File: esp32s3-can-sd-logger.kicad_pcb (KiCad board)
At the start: 4 copper layers, 84 x 74 mm, 168 parts, among them J1 PWR + CAN harness, J10 Sensor harness, J2 USB-C, J3 UART0, J4 I2C / Qwiic, J5 SPI, J6 WS2812, J7 Spare IO, J8 Rail break-out, J9 microSD push-pull, Q1 100V 6.8mOhm N-ch, Q2 -20V 2.3A P-ch, Q3 60V 300mA N-ch, SW1 RESET, SW2 BOOT, U1 LM74700-Q1, U2 LM5164 (5V), U3 LM5164 (3V3), U4 ESP32-S3-WROOM-1-N16R8, U5 USBLC6-2SC6, U6 74AHCT1G125, U7 TJA1051T/3, U8 ADS1115

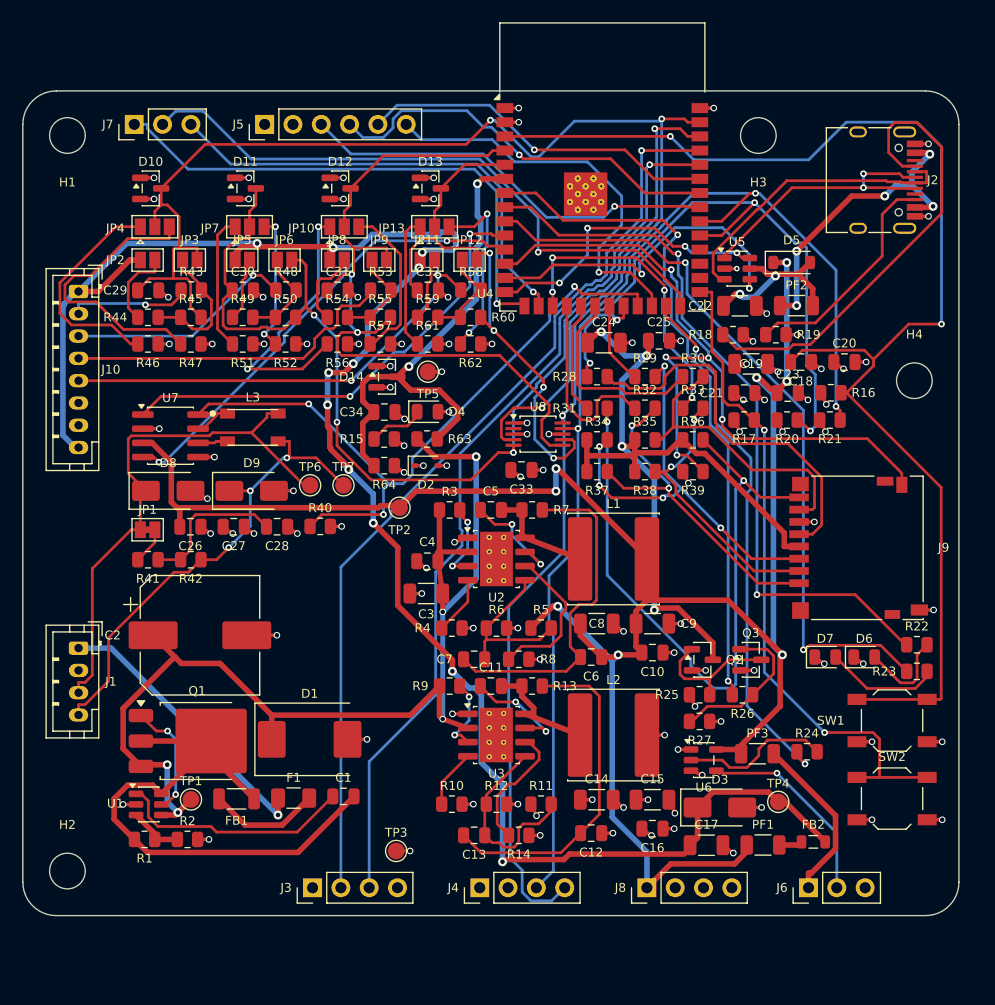
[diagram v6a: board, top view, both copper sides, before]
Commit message: Schematic: power symbols and readable text placement (items 1-2 of 5)
The schematic was a netlist drawn as a picture: 486 global labels for 108
nets, roughly four per net, every part an island with a name flag on each
pin and no wires between anything. You could not trace a circuit by eye.
That is a fair description of a document that fails at the one thing a
schematic is for, and it is on me -- the generator was built to produce a
correct netlist and the drawing was an afterthought.

Two of the five agreed fixes are in:

Rails are power symbols. GND, +3V3, +5V, +5VS, +VBAT, VBUS and SD_VDD now
carry a proper power symbol instead of a net-name label -- 190 of them,
taking the label count from 486 to 296. Where KiCad has no stock symbol
for a rail a generic one is instantiated with its Value overridden, which
is how KiCad names a power net; validate.py re-extracts through KiCad and
compares node-for-node, so a wrong guess there would fail the build rather
than quietly merge two rails. PWR_FLAG keeps a label: pairing it with a
power symbol makes an island of two symbols that declares a rail and
connects to nothing visible.

Text no longer collides. Labels were all justified left, so any label
pointing back at its own component ran its text over the body -- RON_5V
across R4, SW_5V across L1; they now justify away from the part.
Reference and value sat hard against the symbol, so a pin leaving the top
or bottom put its stub and power symbol straight through them: "LM5164
(5V)" printed through the GND symbol under U2. Both now clear the stub,
and the row height accounts for it so the clearance does not just push
the collision into the next row. Power symbol references are hidden, as
they are in every schematic.

Also fixed: the packer wrapped on height but never on width, so the power
sheet silently ran off the 420 mm page -- two symbols landed at x = 422.9
where ERC reported them unconnected and nothing else complained. It now
fails loudly.

Items 3-5 (real hierarchy, w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
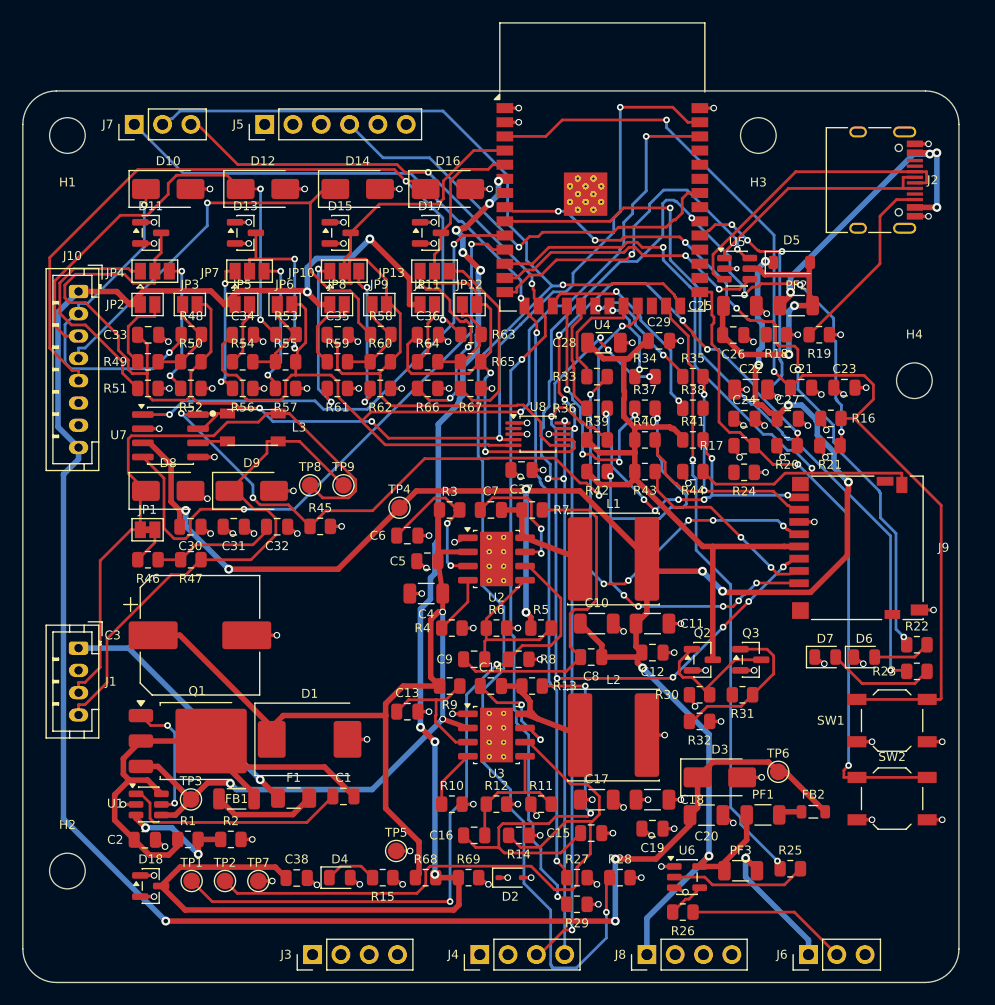
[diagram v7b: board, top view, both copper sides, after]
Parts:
- added C35: 100nF, C_0805_2012Metric, F.Cu at (28.2, 21.9)
- added C36: 100nF, C_0805_2012Metric, F.Cu at (36.3, 21.9)
- added C37: 100nF, C_0805_2012Metric, F.Cu at (44.7, 34.0)
- added C38: 100nF, C_0805_2012Metric, F.Cu at (24.6, 70.6)
- added D15: BAT54S, SOT-23, F.Cu at (28.5, 12.7)
- added D16: SMAJ40CA, D_SMA, F.Cu at (38.1, 8.79)
- added D17: BAT54S, SOT-23, F.Cu at (36.6, 12.7)
- added D18: BAT54S, SOT-23, F.Cu at (11.5, 71.3)
- added R65: 10k, R_0805_2012Metric, F.Cu at (40.2, 24.3)
- added R66: 15k, R_0805_2012Metric, F.Cu at (36.3, 26.7)
- added R67: 2.21k, R_0805_2012Metric, F.Cu at (40.2, 26.7)
- added R68: 100k, R_0805_2012Metric, F.Cu at (36.1, 70.6)
- added R69: 8.2k, R_0805_2012Metric, F.Cu at (40.0, 70.6)
- added TP8: CAN_H, TestPoint_Pad_D1.5mm, F.Cu at (25.8, 35.4)
- added TP9: CAN_L, TestPoint_Pad_D1.5mm, F.Cu at (28.8, 35.4)
- C1: value 1uF 50V -> 1uF
- C10: value 100nF 16V -> 22uF; footprint C_0805_2012Metric -> C_1206_3216Metric
- C11: value 2.2nF 50V -> 22uF; footprint C_0805_2012Metric -> C_1206_3216Metric
- C12: value 3.3nF 50V -> 100nF
- C13: value 270pF 50V -> 10nF
- C14: value 22uF 6.3V -> 2.2nF; footprint C_1206_3216Metric -> C_0805_2012Metric
- C15: value 22uF 6.3V -> 3.3nF; footprint C_1206_3216Metric -> C_0805_2012Metric
- C16: value 100nF 16V -> 270pF
- C17: value 10uF 16V -> 22uF
- C18: value 1uF 16V -> 22uF; footprint C_0805_2012Metric -> C_1206_3216Metric
- C19: value 10uF 16V -> 100nF; footprint C_1206_3216Metric -> C_0805_2012Metric
- C2: value 100uF 100V -> 100nF; footprint CP_Elec_10x10.5 -> C_0805_2012Metric
- C20, C25: value 100nF 16V -> 10uF; footprint C_0805_2012Metric -> C_1206_3216Metric
- C21: value 100nF 16V -> 1uF
- C22: value 10uF 16V -> 10uF
- C23, C26, C27, C29, C30, C31, C33, C34: value 100nF 16V -> 100nF
- C24: value 10uF 6.3V -> 100nF; footprint C_1206_3216Metric -> C_0805_2012Metric
- C28: value 4.7nF 50V -> 10uF; footprint C_0805_2012Metric -> C_1206_3216Metric
- C3: value 10uF 100V -> 100uF; footprint C_1206_3216Metric -> CP_Elec_10x10.5
- C32: value 100nF 16V -> 4.7nF
- C4: value 100nF 100V -> 10uF; footprint C_0805_2012Metric -> C_1206_3216Metric
- C5: value 2.2nF 50V -> 100nF
- C6: value 3.3nF 50V -> 10nF
- C7: value 270pF 50V -> 2.2nF
- C8: value 22uF 16V -> 3.3nF; footprint C_1206_3216Metric -> C_0805_2012Metric
- C9: value 22uF 16V -> 270pF; footprint C_1206_3216Metric -> C_0805_2012Metric
- D1: value SMCJ33A -> SMCJ40A
- D10, D12, D14: value BAT54S -> SMAJ40CA; footprint SOT-23 -> D_SMA
- D3: value SMAJ5.0A -> SMAJ6.0A
- R2: value 25.5k -> 44.2k
- R23: value 1k -> 150
- R24, R28, R29: value 33 -> 10k
- R25: value 100k -> 33
- R26: value 10k -> 100
- R27: value 100k -> 10k
- R30, R32: value 33 -> 100k
- R31: value 33 -> 1k
- R34, R35, R36, R37, R38: value 10k -> 33
- R39: value 47k -> 10k
- R41, R42: value 60.4 -> 10k
- R43: value 1k 0.1% -> 10k
- R44: value 2.49k -> 47k
- R45, R50, R55, R60: value 10k 0.1% -> 10k
- R46: value 15k 0.1% -> 60.4
- R47: value 2.21k 0.1% -> 60.4
- R48, R53, R58: value 1k 0.1% -> 1k
- R51, R56, R61: value 15k 0.1% -> 15k
- R52, R57, R62: value 2.21k 0.1% -> 2.21k
- R63: value 100k -> 1k
- R64: value 10k -> 2.49k
- TP1: value +VBAT -> PG_5V
- TP2: value +5V -> PG_3V3
- TP3: value +3V3 -> +VBAT
- TP4: value +5VS -> +5V
- TP5: value GND -> +3V3
- TP6: value CAN_H -> +5VS
- TP7: value CAN_L -> GND
- moved C26 51.7 mm to (63.7, 21.9)
- moved R44 50.8 mm to (60.1, 34.2)
- moved C27 50.6 mm to (68.6, 29.4)
- moved R41 50.1 mm to (60.1, 31.3)
- moved TP6 49.3 mm to (67.8, 61.1)
- moved R29 47.7 mm to (49.7, 73.0)
- moved C29 46.1 mm to (57.1, 22.4)
- moved R28 45.0 mm to (53.6, 70.6)
- moved R43 43.8 mm to (55.8, 34.2)
- moved TP5 43.1 mm to (33.5, 68.2)
- moved TP4 43.0 mm to (33.8, 37.4)
- moved C19 42.6 mm to (56.5, 66.2)
- moved D4 42.5 mm to (28.4, 70.6)
- moved C20 42.5 mm to (61.3, 65.0)
- moved C18 41.5 mm to (56.5, 63.6)
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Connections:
- C11 pad 1: BST_3V3 -> +5V
- C11 pad 2: SW_3V3 -> GND
- C12 pad 1: RAMP_3V3 -> +5V
- C12 pad 2: +3V3 -> GND
- C13 pad 1: RAMP_3V3 -> EN_3V3
- C13 pad 2: FB_3V3 -> GND
- C14 pad 1: +3V3 -> BST_3V3
- C14 pad 2: GND -> SW_3V3
- C15 pad 1: +3V3 -> RAMP_3V3
- C15 pad 2: GND -> +3V3
- C16 pad 1: +3V3 -> RAMP_3V3
- C16 pad 2: GND -> FB_3V3
- C17 pad 1: +5VS -> +3V3
- C18 pad 1: MCU_EN -> +3V3
- C2 pad 1: +VBAT -> VBAT_FB
- C20 pad 1: +3V3 -> +5VS
- C21 pad 1: +3V3 -> MCU_EN
- C22 pad 1: VBUS -> +3V3
- C23 pad 1: +5V -> +3V3
- C24 pad 1: SD_VDD -> +3V3
- C25 pad 1: SD_VDD -> VBUS
- C26 pad 1: +5V -> VBUS
- C27 pad 1: +3V3 -> +5V
- C28 pad 1: CAN_SPLIT -> SD_VDD
- C29 pad 1: AIN1 -> SD_VDD
- C30 pad 1: AIN2 -> +5V
- C31 pad 1: AIN3 -> +3V3
- C32 pad 1: AIN4 -> CAN_SPLIT
- C33 pad 1: +3V3 -> AIN1
- C34 pad 1: VBAT_SNS -> AIN2
- C5 pad 1: BST_5V -> +VBAT
- C5 pad 2: SW_5V -> GND
- C6 pad 1: RAMP_5V -> EN_5V
- C6 pad 2: +5V -> GND
- C7 pad 1: RAMP_5V -> BST_5V
- C7 pad 2: FB_5V -> SW_5V
- C8 pad 1: +5V -> RAMP_5V
- C8 pad 2: GND -> +5V
- C9 pad 1: +5V -> RAMP_5V
- C9 pad 2: GND -> FB_5V
- D10 pad 1: GND -> AIN1_IN
- D10 pad 2: +3V3 -> GND
- D11 pad 3: AIN2 -> AIN1
- D12 pad 1: GND -> AIN2_IN
- D12 pad 2: +3V3 -> GND
- D13 pad 3: AIN4 -> AIN2
- D14 pad 1: GND -> AIN3_IN
- D14 pad 2: +3V3 -> GND
- J6 pad 2: LED_DIN -> LED_DIN_J
- R24 pad 1: LED_DIN_MCU -> SPI_CS
- R24 pad 2: LED_DIN_A -> +3V3
- R25 pad 1: +3V3 -> LED_DIN_MCU
- R25 pad 2: SD_PG -> LED_DIN_A
- R26 pad 1: SD_PWR_EN -> LED_DIN
- R26 pad 2: SD_EN_G -> LED_DIN_J
- R27 pad 1: SD_EN_G -> IO3
- R28 pad 1: SD_CLK -> IO45
- R28 pad 2: SD_CLK_C -> GND
- R29 pad 1: SD_CMD -> IO46
- R29 pad 2: SD_CMD_C -> GND
- R30 pad 1: SD_D0 -> +3V3
- R30 pad 2: SD_D0_C -> SD_PG
- R31 pad 1: SD_D1 -> SD_PWR_EN
- R31 pad 2: SD_D1_C -> SD_EN_G
- R32 pad 1: SD_D2 -> SD_EN_G
- R32 pad 2: SD_D2_C -> GND
- R33 pad 1: SD_D3 -> SD_CLK
- R33 pad 2: SD_D3_C -> SD_CLK_C
- R34 pad 1: SD_VDD -> SD_CMD
- R35 pad 1: SD_VDD -> SD_D0
- R36 pad 1: SD_VDD -> SD_D1
- R37 pad 1: SD_VDD -> SD_D2
- R38 pad 1: SD_VDD -> SD_D3
- R39 pad 1: +3V3 -> SD_VDD
- R39 pad 2: SD_CD -> SD_CMD_C
- R40 pad 1: CAN_S -> SD_VDD
- R40 pad 2: GND -> SD_D0_C
- R41 pad 1: TERM_A -> SD_VDD
- R41 pad 2: CAN_SPLIT -> SD_D1_C
- R42 pad 1: CAN_SPLIT -> SD_VDD
- R42 pad 2: CAN_L -> SD_D2_C
- R43 pad 1: AIN1_IN -> SD_VDD
- R43 pad 2: AIN1_A -> SD_D3_C
- R44 pad 1: AIN1_PU -> +3V3
- R44 pad 2: AIN1_A -> SD_CD
- R45 pad 1: AIN1_A -> CAN_S
- R45 pad 2: AIN1 -> GND
- R46 pad 1: AIN1_R1 -> TERM_A
- R46 pad 2: GND -> CAN_SPLIT
- R47 pad 1: AIN1_R2 -> CAN_SPLIT
- R47 pad 2: GND -> CAN_L
- R48 pad 1: AIN2_IN -> AIN1_IN
- R48 pad 2: AIN2_A -> AIN1_A
- R49 pad 1: AIN2_PU -> AIN1_PU
- R49 pad 2: AIN2_A -> AIN1_A
- R50 pad 1: AIN2_A -> AIN1_A
- R50 pad 2: AIN2 -> AIN1
- R51 pad 1: AIN2_R1 -> AIN1_R1
- R52 pad 1: AIN2_R2 -> AIN1_R2
- R53 pad 1: AIN3_IN -> AIN2_IN
- R53 pad 2: AIN3_A -> AIN2_A
- R54 pad 1: AIN3_PU -> AIN2_PU
- R54 pad 2: AIN3_A -> AIN2_A
- R55 pad 1: AIN3_A -> AIN2_A
- R55 pad 2: AIN3 -> AIN2
- R56 pad 1: AIN3_R1 -> AIN2_R1
- R57 pad 1: AIN3_R2 -> AIN2_R2
- R58 pad 1: AIN4_IN -> AIN3_IN
- R58 pad 2: AIN4_A -> AIN3_A
- R59 pad 1: AIN4_PU -> AIN3_PU
- R59 pad 2: AIN4_A -> AIN3_A
- R60 pad 1: AIN4_A -> AIN3_A
- R60 pad 2: AIN4 -> AIN3
- R61 pad 1: AIN4_R1 -> AIN3_R1
- R62 pad 1: AIN4_R2 -> AIN3_R2
- R63 pad 1: +VBAT -> AIN4_IN
- R63 pad 2: VBAT_SNS -> AIN4_A
- R64 pad 1: VBAT_SNS -> AIN4_PU
- R64 pad 2: GND -> AIN4_A
- TP1 pad 1: +VBAT -> PG_5V
- TP2 pad 1: +5V -> PG_3V3
- TP3 pad 1: +3V3 -> +VBAT
- TP4 pad 1: +5VS -> +5V
- TP5 pad 1: GND -> +3V3
- TP6 pad 1: CAN_H -> +5VS
- TP7 pad 1: CAN_L -> GND
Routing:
- net UART_TX: track 83.1 -> 0.00 mm, vias 1 -> 0
- net UART_RX: track 80.5 -> 0.00 mm, vias 1 -> 0
- net IO45: track 56.8 -> 135.2 mm, vias 1 -> 2
- net VBAT_SNS: track 45.3 -> 112.4 mm, vias 2 -> 8
- net SD_PWR_EN: track 61.4 -> 0.00 mm, vias 2 -> 0
- net IO46: track 42.3 -> 93.3 mm, vias 1 -> 4
- net PG_3V3: track 11.4 -> 61.1 mm
- net PG_5V: track 13.7 -> 61.6 mm, vias 0 -> 2
- net IO3: track 47.9 -> 92.3 mm, vias 1 -> 3
- net USB_CC1: track 42.1 -> 0.00 mm
- net SPI_SCK: track 37.9 -> 0.00 mm, vias 1 -> 0
- net SPI_CS: track 36.3 -> 0.00 mm, vias 1 -> 0
- net SD_D1_C: track 60.5 -> 27.6 mm, vias 2 -> 7
- net SPI_MOSI: track 32.3 -> 0.00 mm, vias 1 -> 0
- net SD_CMD_C: track 38.0 -> 69.5 mm, vias 5 -> 9
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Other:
- board size 84 x 74 mm -> 84 x 80 mm

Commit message: Rev B board: netclass fix for the sense nodes, and a floor under rip-up
Two real faults, both of the kind that pass DRC while being wrong.

VBAT_UVLO and VBAT_SNS were being routed at 0.5 mm. The netclass pattern
"VBAT_*" swept them into the Power class along with the three nets that
actually carry battery current. Neither of them carries any: VBAT_UVLO is
the LM74700 enable divider midpoint and VBAT_SNS is the ADC sense node,
both high-impedance at microamps. Wide copper there is wasted, couples
more noise onto an analog node, and made a 63 mm run across a congested
board far harder than it needed to be. Replaced with explicit patterns
for VBAT_IN, VBAT_F and VBAT_FB.

maze_route could make the board worse and did: one run took it from 4
open connections to 13, having ripped out more than it could put back.
It now scores the board before it starts, keeps the best state it has
seen, and restores that if the final result is worse. On the very next
run the guard fired and saved a board that had reached 3 open from a
pass that would have left it at 6. A --no-rip mode was added alongside,
and it earned its place immediately as a diagnostic: with rip-up off the
router reports "no path" honestly instead of buying a route by wrecking
four other nets, which is what sent me looking at the netclasses.

Footprint keepouts now reach the autorouter, so the track freerouting
had been running through the middle of the microSD card slot is gone.

State: 0 DRC errors, 3 unconnected, 149 placed parts, 84 x 80 mm. The
last three are ordinary connections in congested space; the automated
pipeline oscillates between two and three of them across runs and is not
converging further. They want the interactive router, as Rev A's last
three did.

Co-Authored-By: Claude Opus 5 <noreply@anthropic.com>
Claude-Session: https://claude.ai/code/session_01DhNbL25h25p8VFCjRfJik9
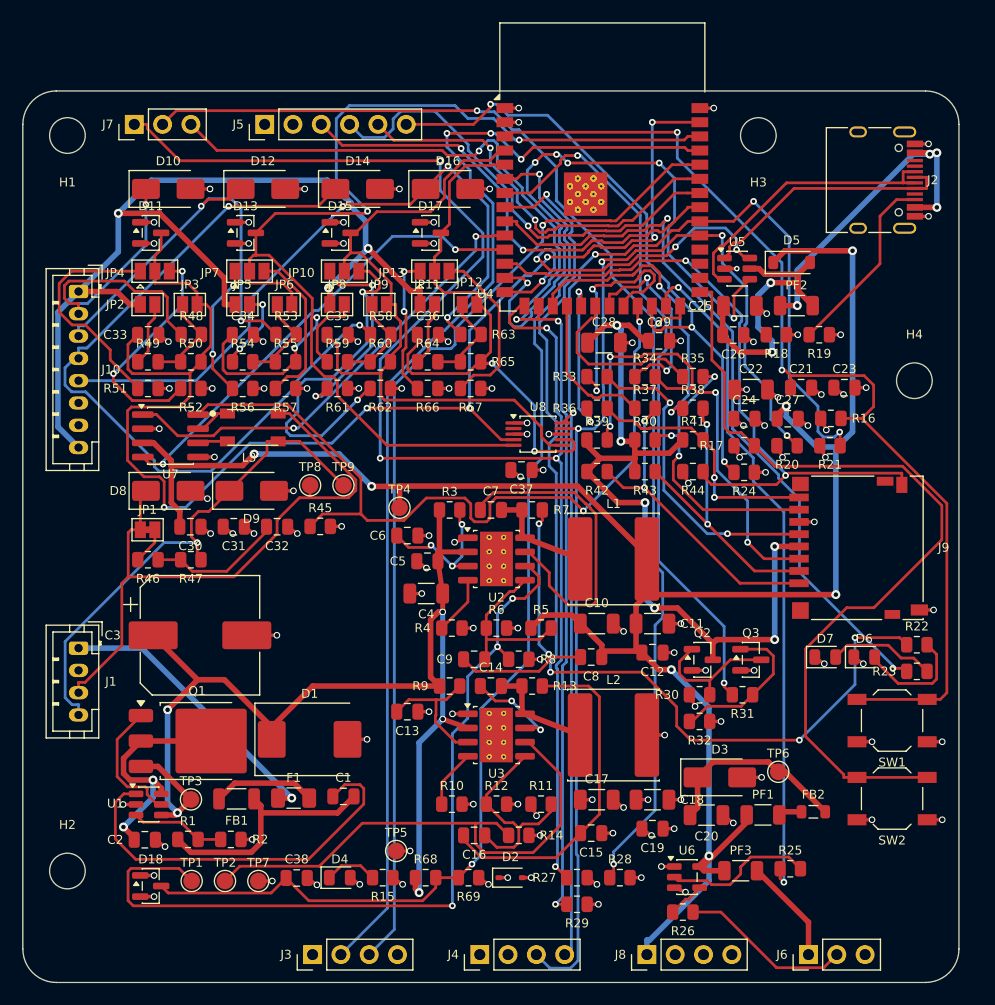
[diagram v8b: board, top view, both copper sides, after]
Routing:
- net UART_TX: track 0.00 -> 105.4 mm, vias 0 -> 3
- net UART_RX: track 0.00 -> 89.3 mm, vias 0 -> 1
- net +5VS: track 178.9 -> 104.6 mm, vias 5 -> 3
- net SD_PWR_EN: track 0.00 -> 62.9 mm, vias 0 -> 2
- net SPI_CS: track 0.00 -> 58.7 mm, vias 0 -> 3
- net SPI_SCK: track 0.00 -> 42.7 mm, vias 0 -> 2
- net IO3: track 92.3 -> 133.7 mm, vias 3 -> 5
- net SPI_MOSI: track 0.00 -> 36.7 mm, vias 0 -> 2
- net USB_DM: track 25.0 -> 59.0 mm, vias 2 -> 6
- net LED1: track 62.4 -> 93.1 mm, vias 6 -> 4
- net SD_CMD_C: track 69.5 -> 43.2 mm, vias 9 -> 4
- net IO45: track 135.2 -> 111.2 mm, vias 2 -> 3
- net AIN3_IN: track 46.2 -> 70.1 mm, vias 1 -> 2
- net BST_5V: track 11.7 -> 29.1 mm, vias 2 -> 0
- net AIN3_R2: track 13.7 -> 30.9 mm
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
